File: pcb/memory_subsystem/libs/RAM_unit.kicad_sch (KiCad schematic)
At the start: 6 parts, among them U3 74LS245

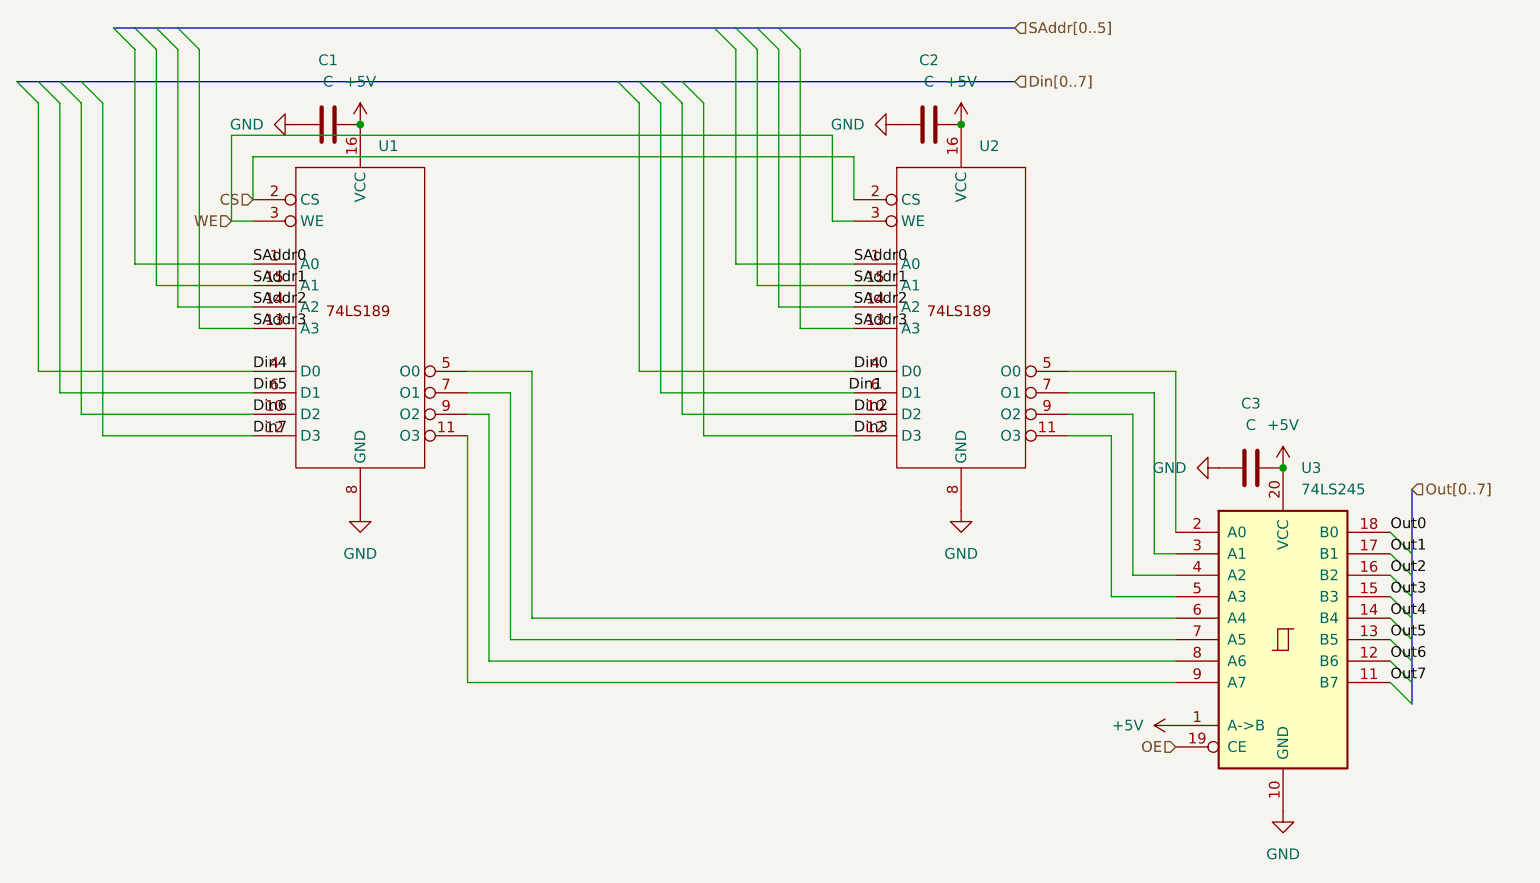
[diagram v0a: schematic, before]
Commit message: Finished first draft of memory subsystem
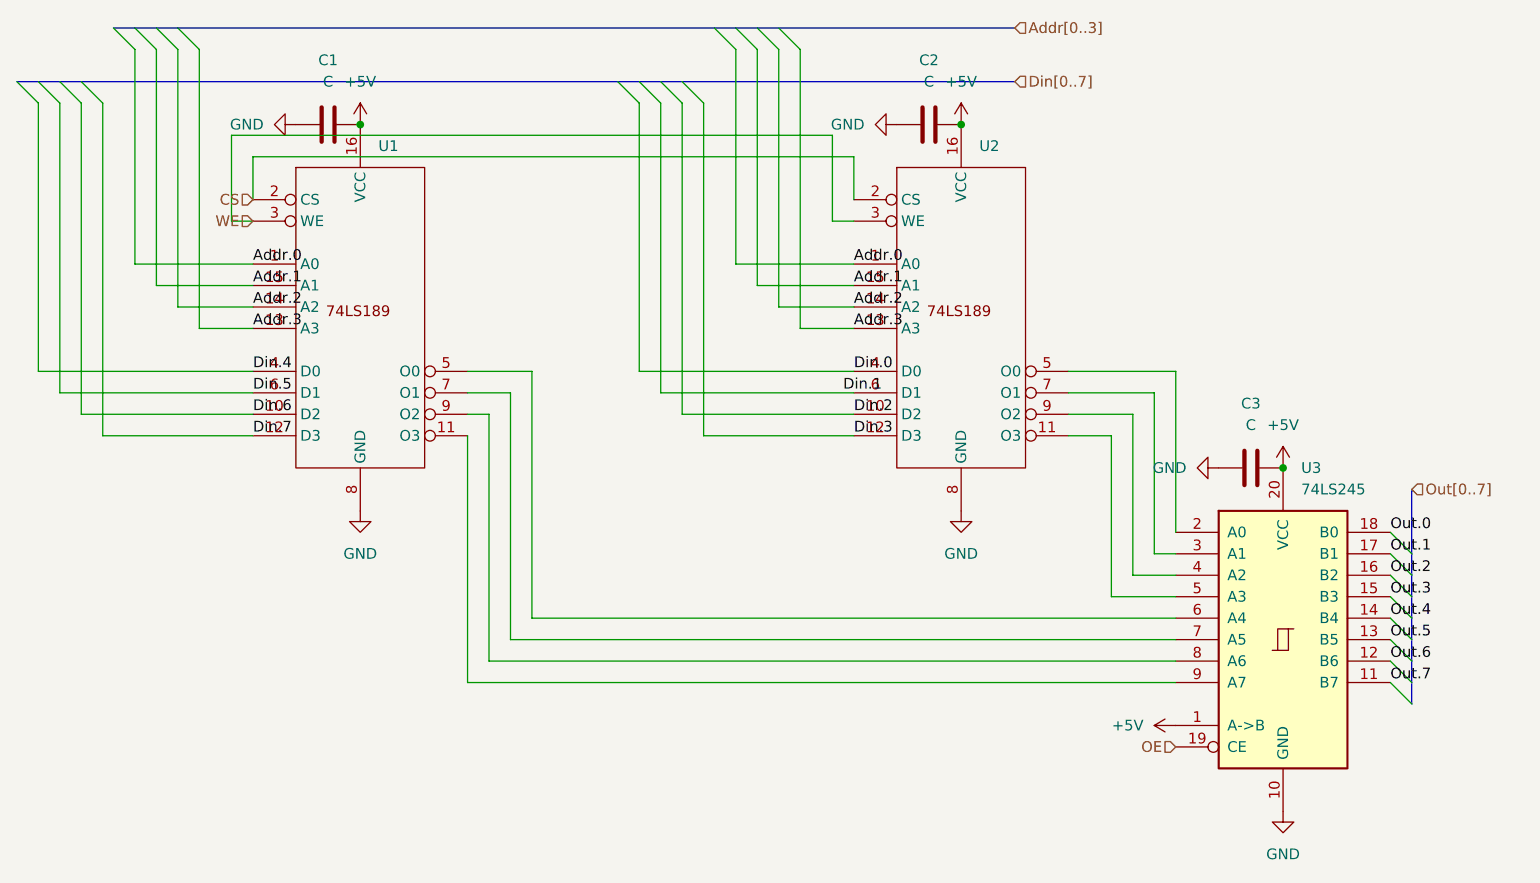
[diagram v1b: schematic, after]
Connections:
- net Din0 renamed Din.0
- net Din1 renamed Din.1
- net Din2 renamed Din.2
- net Din3 renamed Din.3
- net Din4 renamed Din.4
- net Din5 renamed Din.5
- net Din6 renamed Din.6
- net Din7 renamed Din.7
- net Out0 renamed Out.0
- net Out1 renamed Out.1
- net Out2 renamed Out.2
- net Out3 renamed Out.3
- net Out4 renamed Out.4
- net Out5 renamed Out.5
- net Out6 renamed Out.6
- net Out7 renamed Out.7
- net SAddr0 renamed Addr.0
- net SAddr1 renamed Addr.1
- net SAddr2 renamed Addr.2
- net SAddr3 renamed Addr.3
